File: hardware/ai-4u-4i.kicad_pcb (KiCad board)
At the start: 4 copper layers, 100 x 85 mm, 164 parts, among them J101 TNG-Power-TOP, J102 TNG-Power-BTM, J103 TNG-Data-TOP, J104 TNG-Data-BTM, P102 Debug, P103 PE, P201 INPUT0, P202 INPUT1, P203 INPUT2, P204 INPUT3, Q101 FDS8449, SW101 BOOT, T101 744273222, U101 STM32F070CBT6, U102 AZ1117EH, U103 82400152, U104 TEL10, U105 TLP293, U106 STEF01, U203 ISO7741DWR, U205 TPS7A6633QDGNRQ1, X101 TBD

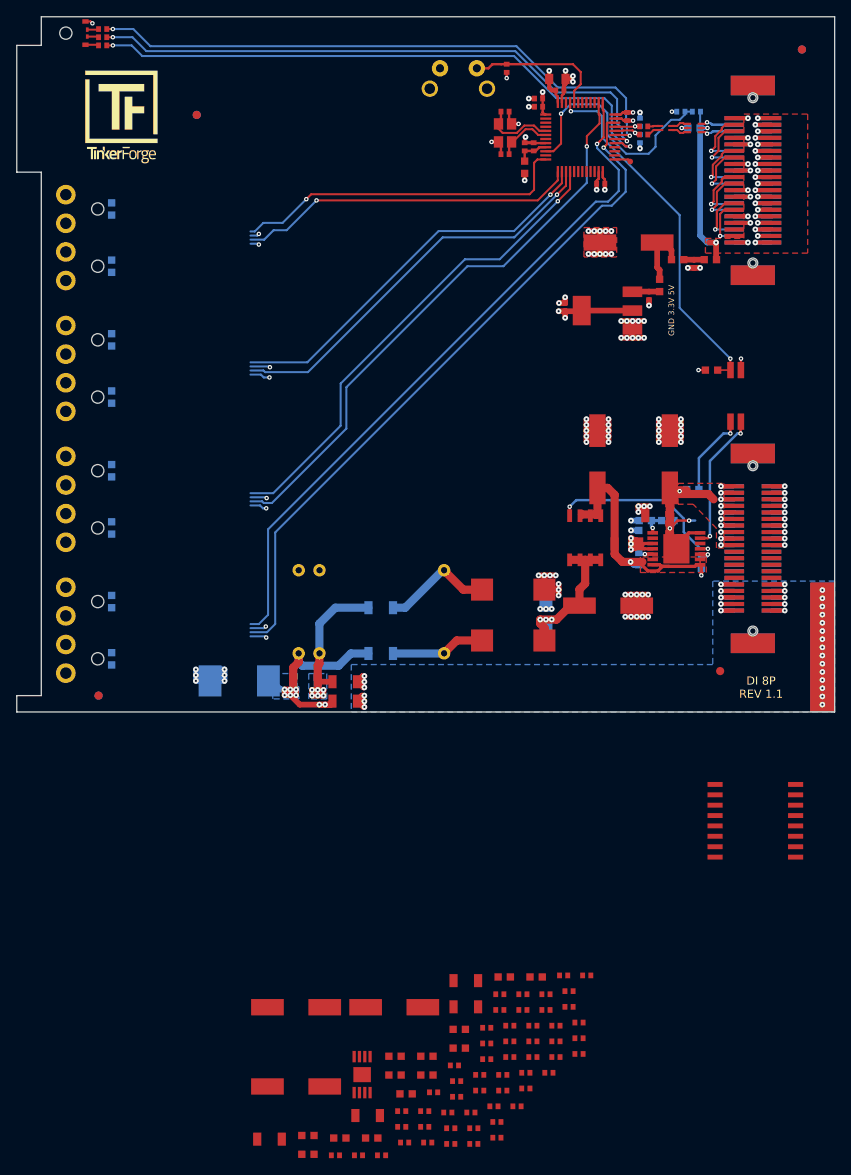
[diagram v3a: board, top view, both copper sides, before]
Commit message: placement finished, some routing
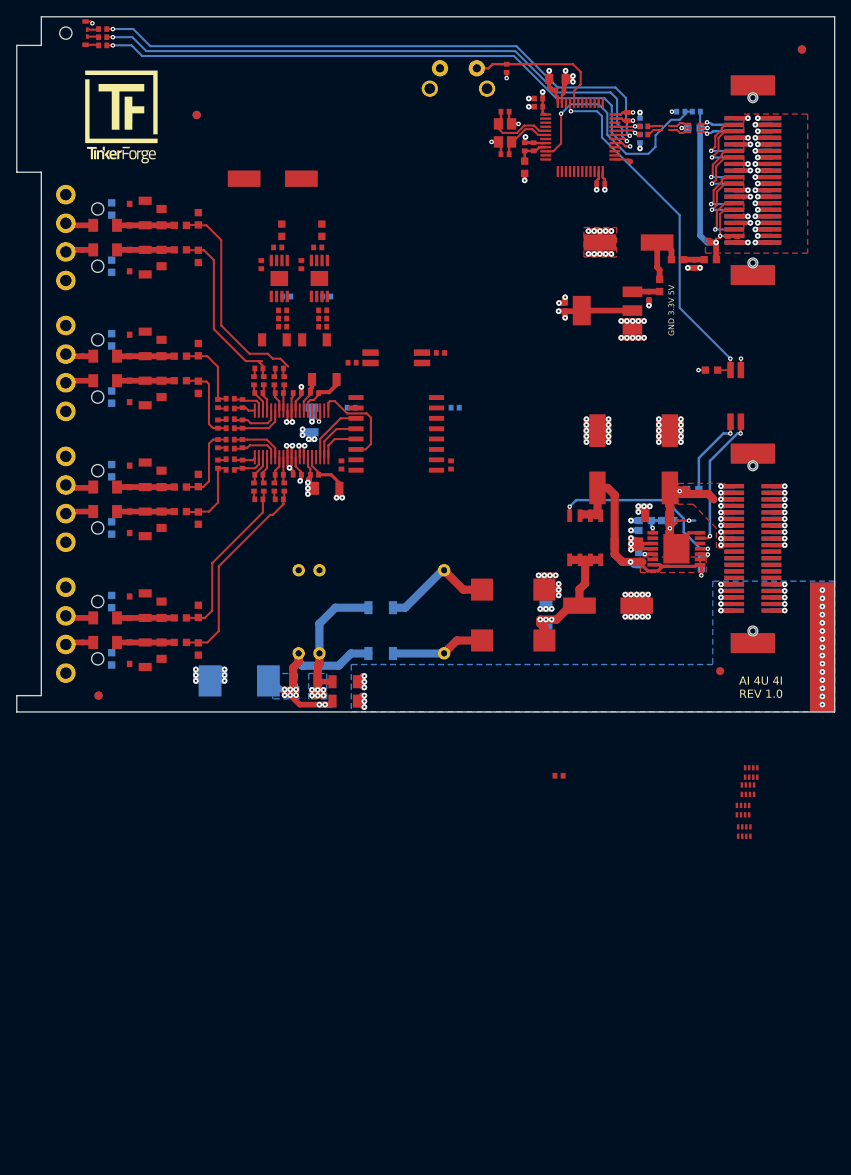
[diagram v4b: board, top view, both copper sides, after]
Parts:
- removed C247: TBD, kicad-libraries:ELKO_83
- added C202: 27nF, kicad-libraries:C1206, F.Cu at (105.5, 92.5)
- added C203: 27nF, kicad-libraries:C1206, F.Cu at (105.5, 102.5)
- added C204: 27nF, kicad-libraries:C1206, F.Cu at (105.5, 108.5)
- added C205: 27nF, kicad-libraries:C1206, F.Cu at (105.5, 118.5)
- added C206: 27nF, kicad-libraries:C1206, F.Cu at (105.5, 124.5)
- added C207: 27nF, kicad-libraries:C1206, F.Cu at (105.5, 134.5)
- added C208: 27nF, kicad-libraries:C1206, F.Cu at (105.5, 140.5)
- added C209: 2700pF, kicad-libraries:C0603F, F.Cu at (112.0, 87.2)
- added C210: 2700pF, kicad-libraries:C0603F, F.Cu at (112.0, 91.8)
- added C211: 2700pF, kicad-libraries:C0603F, F.Cu at (112.0, 103.2)
- added C212: 2700pF, kicad-libraries:C0603F, F.Cu at (112.0, 107.8)
- added C213: 2700pF, kicad-libraries:C0603F, F.Cu at (112.0, 119.2)
- added C225: 22uF, kicad-libraries:C1206, F.Cu at (126.2, 102.0)
- added D201: CDSOD323-T12C, kicad-libraries:SOD-323, F.Cu at (103.6, 86.7)
- added D202: CDSOD323-T12C, kicad-libraries:SOD-323, F.Cu at (103.6, 92.3)
- added D211: CDSOD323-T12C, kicad-libraries:SOD-323, F.Cu at (103.6, 102.7)
- added D212: CDSOD323-T12C, kicad-libraries:SOD-323, F.Cu at (103.6, 108.3)
- added D213: CDSOD323-T12C, kicad-libraries:SOD-323, F.Cu at (103.6, 118.7)
- added D214: CDSOD323-T12C, kicad-libraries:SOD-323, F.Cu at (103.6, 124.3)
- added D215: CDSOD323-T12C, kicad-libraries:SOD-323, F.Cu at (103.6, 134.7)
- added D216: CDSOD323-T12C, kicad-libraries:SOD-323, F.Cu at (103.6, 140.3)
- added R201: 100, kicad-libraries:RMELF, F.Cu at (100.6, 88.0)
- added R202: 100, kicad-libraries:RMELF, F.Cu at (100.6, 91.0)
- added R203: 100, kicad-libraries:RMELF, F.Cu at (100.6, 104.0)
- added R204: 100, kicad-libraries:RMELF, F.Cu at (100.6, 107.0)
- added R205: 100, kicad-libraries:RMELF, F.Cu at (100.6, 120.0)
- added R206: 100, kicad-libraries:RMELF, F.Cu at (100.6, 123.0)
- added R207: 100, kicad-libraries:RMELF, F.Cu at (100.6, 136.0)
- added R208: 100, kicad-libraries:RMELF, F.Cu at (100.6, 139.0)
- added R209: DNP, kicad-libraries:R0805, F.Cu at (107.5, 87.0)
- added R210: 124, kicad-libraries:R0805, F.Cu at (107.5, 92.0)
- added R211: DNP, kicad-libraries:R0805, F.Cu at (107.5, 103.0)
- added R212: 124, kicad-libraries:R0805, F.Cu at (107.5, 108.0)
- added R213: DNP, kicad-libraries:R0805, F.Cu at (107.5, 119.0)
- added R214: 124, kicad-libraries:R0805, F.Cu at (107.5, 124.0)
- added R215: DNP, kicad-libraries:R0805, F.Cu at (107.5, 135.0)
- added R216: 124, kicad-libraries:R0805, F.Cu at (107.5, 140.0)
- added RP201: 470, kicad-libraries:4X0402, F.Cu at (179.6, 154.9)
- added RP202: 470, kicad-libraries:4X0402, F.Cu at (178.8, 162.1)
- added RP203: 470, kicad-libraries:4X0402, F.Cu at (179.2, 157.0)
- added RP204: 470, kicad-libraries:4X0402, F.Cu at (178.6, 159.5)
- added U201: ADS8698, kicad-libraries:TSSOP38, F.Cu at (123.4, 113.5)
- added U202: TLP293, kicad-libraries:SOP4, F.Cu at (136.2, 104.2)
- added U204: TPS7A6650QDGNRQ1, kicad-libraries:MSOP-8-EP, F.Cu at (126.8, 94.5)
- C231, R252, R254, R256, R257: moved to B.Cu
- C246: value TBD -> 22uF; footprint kicad-libraries:ELKO_83 -> kicad-libraries:C1206
- moved R218 111.7 mm to (109.8, 91.0), turned to 180 degrees
- moved C239 109.9 mm to (119.7, 92.8), turned to 90 degrees
- moved R217 107.2 mm to (109.8, 88.0), turned to 180 degrees
- moved C201 104.7 mm to (105.5, 86.5), turned to 90 degrees
- moved C238 104.6 mm to (124.6, 92.8), turned to 90 degrees
- moved L201 101.4 mm to (127.1, 88.6), turned to 90 degrees
- moved C234 101.3 mm to (121.1, 82.3)
- moved C245 99.4 mm to (122.3, 100.4)
- moved R257 98.1 mm to (122.8, 96.7), turned to 180 degrees
- moved U205 97.9 mm to (121.9, 94.5), turned to 180 degrees
- moved C236 97.6 mm to (126.6, 90.7)
- moved C237 97.1 mm to (121.7, 90.7)
- moved R253 96.7 mm to (141.6, 103.6), turned to 180 degrees
- moved R225 95.9 mm to (121.9, 105.5)
- moved L202 95.3 mm to (122.2, 88.6), turned to 90 degrees
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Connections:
- C217 pad 1: AIN0_P -> AIN6_P
- C217 pad 2: AIN0_N -> AIN6_N
- C218 pad 1: AIN1_P -> AIN0_P
- C218 pad 2: AIN1_N -> AIN0_N
- C219 pad 1: AIN2_P -> AIN1_P
- C219 pad 2: AIN2_N -> AIN1_N
- C220 pad 1: AIN3_P -> AIN7_P
- C220 pad 2: AIN3_N -> AIN7_N
- C222 pad 1: AIN5_P -> AIN2_P
- C222 pad 2: AIN5_N -> AIN2_N
- C223 pad 1: AIN6_P -> AIN3_P
- C223 pad 2: AIN6_N -> AIN3_N
- C224 pad 1: AIN7_P -> AIN5_P
- C224 pad 2: AIN7_N -> AIN5_N
- C246 pad 1: AVDD -> DVDD
- R233 pad 1: AIN0_P -> AIN6_P
- R234 pad 1: AIN0_N -> AIN6_N
- R235 pad 1: AIN1_P -> AIN0_P
- R236 pad 1: AIN1_N -> AIN0_N
- R237 pad 1: AIN2_P -> AIN1_P
- R238 pad 1: AIN2_N -> AIN1_N
- R239 pad 1: AIN3_P -> AIN7_P
- R240 pad 1: AIN3_N -> AIN7_N
- R243 pad 1: AIN5_P -> AIN2_P
- R244 pad 1: AIN5_N -> AIN2_N
- R245 pad 1: AIN6_P -> AIN3_P
- R246 pad 1: AIN6_N -> AIN3_N
- R247 pad 1: AIN7_P -> AIN5_P
- R248 pad 1: AIN7_N -> AIN5_N
- U203 pad 4: SPI-CLK -> SPI-CS
- U203 pad 5: SPI-CS -> SPI-CLK
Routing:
- net LED7: track 85.4 -> 0.00 mm, vias 1 -> 0
- net LED6: track 85.4 -> 0.00 mm, vias 1 -> 0
- net SPI-CS: track 70.9 -> 0.00 mm, vias 1 -> 0
- net LED4: track 59.6 -> 0.00 mm, vias 1 -> 0
- net LED3: track 49.8 -> 0.00 mm, vias 1 -> 0
- net LED2: track 48.6 -> 0.00 mm, vias 1 -> 0
- net AGND: track 33.0 -> 75.8 mm, vias 12 -> 27
- net LED0: track 41.7 -> 0.00 mm, vias 1 -> 0
- net LED1: track 41.7 -> 0.00 mm, vias 1 -> 0
- net Net-(C209-Pad1): track 0.00 -> 27.2 mm
- net Net-(C216-Pad1): track 0.00 -> 25.3 mm
- net Net-(C210-Pad1): track 0.00 -> 22.1 mm
- net Net-(C215-Pad1): track 0.00 -> 21.0 mm
- net 3V3: track 39.8 -> 24.7 mm, vias 17 -> 9
- net Net-(U201-Pad1): track 0.00 -> 12.4 mm
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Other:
- board text added: "AI 4U 4I REV 1.0"
- board text added: "AI0"
- board text added: "AI1"
- board text added: "AI2"
- board text added: "AI3"
- board text added: "AI4"
- board text added: "AI5"
- board text added: "AI6"
- board text added: "AI7"
- board text removed: "DI 8P REV 1.1"
- board text removed: "DI0"
- board text removed: "DI1"
- board text removed: "DI2"
- board text removed: "DI3"
- board text removed: "DI4"
- board text removed: "DI5"
- board text removed: "DI6"
- board text removed: "DI7"

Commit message: fully routed
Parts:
- removed R255: 47, kicad-libraries:R0402F
- added RP206: 470, kicad-libraries:4X0402, F.Cu at (144.4, 113.5)
- RP201, RP202, RP203, RP204: moved to B.Cu
- moved RP201 76.5 mm to (140.0, 89.4), turned to 270 degrees
- moved RP202 68.7 mm to (140.0, 105.4), turned to 270 degrees
- moved RP203 53.0 mm to (140.0, 121.4), turned to 270 degrees
- moved RP204 51.2 mm to (140.0, 125.9), turned to 270 degrees
- moved L201 4.90 mm to (122.2, 88.7)
- moved L202 4.90 mm to (127.1, 88.7)
- moved C240 4.90 mm to (122.3, 98.5)
- moved C241 4.90 mm to (127.2, 98.5)
- moved C242 4.90 mm to (122.3, 99.5)
- moved C243 4.90 mm to (127.2, 99.5)
- moved C244 4.90 mm to (122.3, 100.5)
- moved C245 4.90 mm to (127.2, 100.5)
- moved R256 4.90 mm to (122.8, 96.7)
- moved R257 4.90 mm to (127.7, 96.7)
- moved C236 4.90 mm to (121.7, 90.7)
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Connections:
- U101 pad 11: (no net) -> ADC-RESET
- U101 pad 18: (no net) -> LED6
- U101 pad 19: (no net) -> LED7
- U101 pad 34: LED7 -> (no net)
- U101 pad 37: LED6 -> (no net)
- U101 pad 42: ADC-RESET -> (no net)
- U203 pad 3: SPI-MOSI -> Net-(RP206-Pad8)
- U203 pad 4: SPI-CS -> Net-(RP206-Pad7)
- U203 pad 5: SPI-CLK -> Net-(RP206-Pad6)
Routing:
- net AGND: track 75.8 -> 252.6 mm, vias 27 -> 160
- net LED7: track 0.00 -> 54.6 mm, vias 0 -> 1
- net LED6: track 0.00 -> 53.3 mm, vias 0 -> 1
- net LED5: track 0.00 -> 50.0 mm, vias 0 -> 1
- net LED4: track 0.00 -> 48.8 mm, vias 0 -> 1
- net SPI-CS: track 0.00 -> 48.6 mm, vias 0 -> 2
- net SPI-MOSI: track 0.00 -> 48.4 mm, vias 0 -> 2
- net SPI-CLK: track 0.00 -> 47.7 mm, vias 0 -> 2
- net Net-(D210-Pad1): track 0.00 -> 46.9 mm
- net SPI-MISO: track 0.00 -> 46.9 mm, vias 0 -> 2
- net Net-(D209-Pad2): track 0.00 -> 46.2 mm
- net Net-(D210-Pad2): track 0.00 -> 46.2 mm
- net Net-(D209-Pad1): track 0.00 -> 45.6 mm
- net Net-(D206-Pad1): track 0.00 -> 41.0 mm
- net Net-(D207-Pad2): track 0.00 -> 40.9 mm
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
